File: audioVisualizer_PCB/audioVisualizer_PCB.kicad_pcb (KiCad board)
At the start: 2 copper layers, 129.1 x 32.5 mm, 40 parts, among them J1 USB_C_16P, J2 SWD_DEBUG, J3 SPI_LED_MATRIX, U1 AMS1117-3.3, U7 STM32F401CCUx, Y1 ASE-25MHz

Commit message: update
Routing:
- net +3.3V: track 322.8 -> 296.7 mm, vias 7 -> 9
- net GND: track 129.1 -> 124.5 mm, vias 22 -> 21
- net SWDIO: track 16.9 -> 15.7 mm

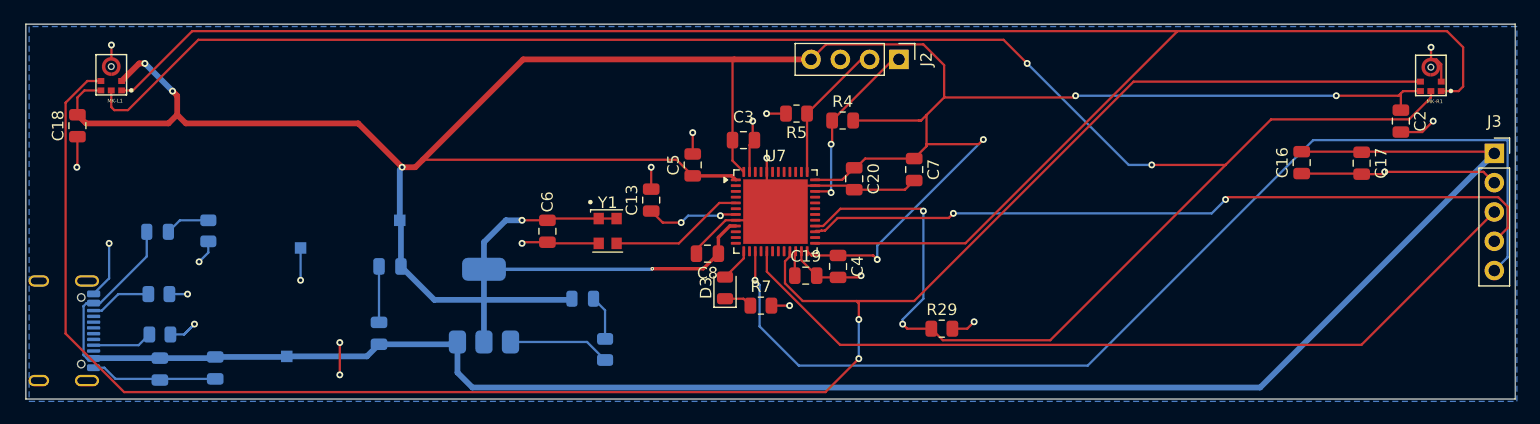
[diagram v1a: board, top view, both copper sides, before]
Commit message: update afer review; power fixed?
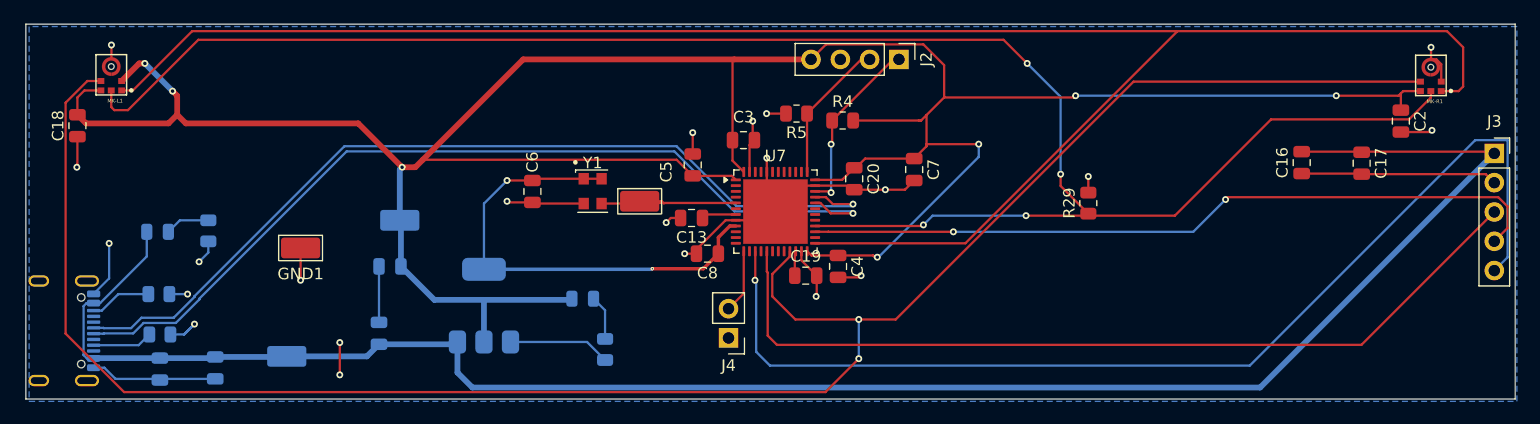
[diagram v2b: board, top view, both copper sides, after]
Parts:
- removed D3: LED, LED_SMD:LED_0805_2012Metric
- removed R7: 10Ω, Resistor_SMD:R_0805_2012Metric
- added CRYS_25: CRYS_25, TestPoint:TestPoint_Keystone_5015_Micro_Mini, F.Cu at (90.9, 65.0)
- added J4: test_con, Connector_PinHeader_2.54mm:PinHeader_1x02_P2.54mm_Vertical, F.Cu at (98.6, 76.8)
- 3V3, 5V1: footprint TestPoint:TestPoint_Pad_1.0x1.0mm -> TestPoint:TestPoint_Keystone_5015_Micro_Mini
- C13: value 100n -> 100nF
- GND1: footprint TestPoint:TestPoint_Pad_1.0x1.0mm -> TestPoint:TestPoint_Keystone_5015_Micro_Mini; moved to F.Cu
- R1, R3: value 5.1 -> 5.1k
- moved R29 16.7 mm to (129.8, 65.1), turned to 90 degrees
- moved C13 3.83 mm to (95.4, 66.4), turned to 180 degrees
- moved C6 3.69 mm to (81.6, 64.1)
- moved Y1 3.69 mm to (86.8, 64.1)
- turned GND1 to 180 degrees
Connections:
- J1 pad A6: unconnected-(J1-D+-PadA6) -> USB_D+
- J1 pad A7: unconnected-(J1-D--PadA7) -> USB_D-
- J1 pad B6: unconnected-(J1-D+-PadA6) -> USB_D+
- J1 pad B7: unconnected-(J1-D--PadA7) -> USB_D-
- U7 pad 32: unconnected-(U7-PA11-Pad32) -> USB_D+
- U7 pad 33: unconnected-(U7-PA12-Pad33) -> USB_D-
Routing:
- net USB_D+: track 0.00 -> 78.3 mm, vias 0 -> 1
- net USB_D-: track 0.00 -> 78.2 mm, vias 0 -> 1
- net MIC_SD: track 181.5 -> 158.1 mm
- net Net-(U7-NRST): track 8.04 -> 3.01 mm, vias 2 -> 0
- net SPI_DIN: track 72.2 -> 75.5 mm
- net Net-(J4-Pin_2): track 2.91 -> 5.53 mm
- net Net-(D3-K): track 2.45 -> 0.00 mm
- net GND: track 124.5 -> 122.1 mm, vias 21 -> 22
- net /CRYS_OUT: track 11.8 -> 14.0 mm
- net +3.3V: track 296.7 -> 294.6 mm
- net MIC_SCK: track 167.6 -> 169.5 mm
- net SPI_CLK: track 92.8 -> 94.3 mm

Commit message: update
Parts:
- removed J4: test_con, Connector_PinHeader_2.54mm:PinHeader_1x02_P2.54mm_Vertical
- removed U7: STM32F401CCUx, Package_DFN_QFN:QFN-48-1EP_7x7mm_P0.5mm_EP5.6x5.6mm
- added U2: STM32F401RETx, Package_QFP:LQFP-64_10x10mm_P0.5mm, F.Cu at (106.2, 67.8)
- moved C4 28.3 mm to (136.3, 72.5)
- moved C19 28.3 mm to (133.5, 73.3)
- moved R29 27.4 mm to (105.8, 51.8)
- moved J2 23.1 mm to (122.4, 73.9), turned to 180 degrees
- moved C20 17.8 mm to (126.9, 59.2)
- moved C7 17.8 mm to (132.1, 58.5)
- moved R4 17.8 mm to (125.9, 54.2)
- moved R5 17.8 mm to (121.9, 53.6)
- moved C5 16.9 mm to (103.2, 76.8), turned to 180 degrees
- moved CRYS_25 11.4 mm to (82.9, 56.9)
- moved Y1 11.4 mm to (78.8, 56.0)
- moved C6 11.4 mm to (73.6, 56.0)
- moved C8 8.06 mm to (98.4, 61.6), turned to 90 degrees
- moved C3 3.79 mm to (103.4, 58.2)
- moved R2 3.52 mm to (84.4, 78.2)
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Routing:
- net +3.3V: track 294.6 -> 0.00 mm, vias 9 -> 0
- net MIC_SCK: track 169.5 -> 0.00 mm, vias 2 -> 0
- net +5V: track 165.1 -> 0.00 mm
- net MIC_WS: track 163.5 -> 0.00 mm
- net MIC_SD: track 158.1 -> 0.00 mm, vias 4 -> 0
- net GND: track 122.1 -> 0.00 mm, vias 22 -> 0
- net SPI_CLK: track 94.3 -> 0.00 mm, vias 1 -> 0
- net USB_D+: track 78.3 -> 0.00 mm, vias 1 -> 0
- net USB_D-: track 78.2 -> 0.00 mm, vias 1 -> 0
- net SPI_DIN: track 75.5 -> 0.00 mm
- net SPI_CS: track 65.1 -> 0.00 mm, vias 2 -> 0
- net SWDIO: track 15.7 -> 0.00 mm, vias 2 -> 0
- net /CRYS_OUT: track 14.0 -> 0.00 mm
- net SWCLK: track 12.5 -> 0.00 mm
- net Net-(J4-Pin_2): track 5.53 -> 0.00 mm
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
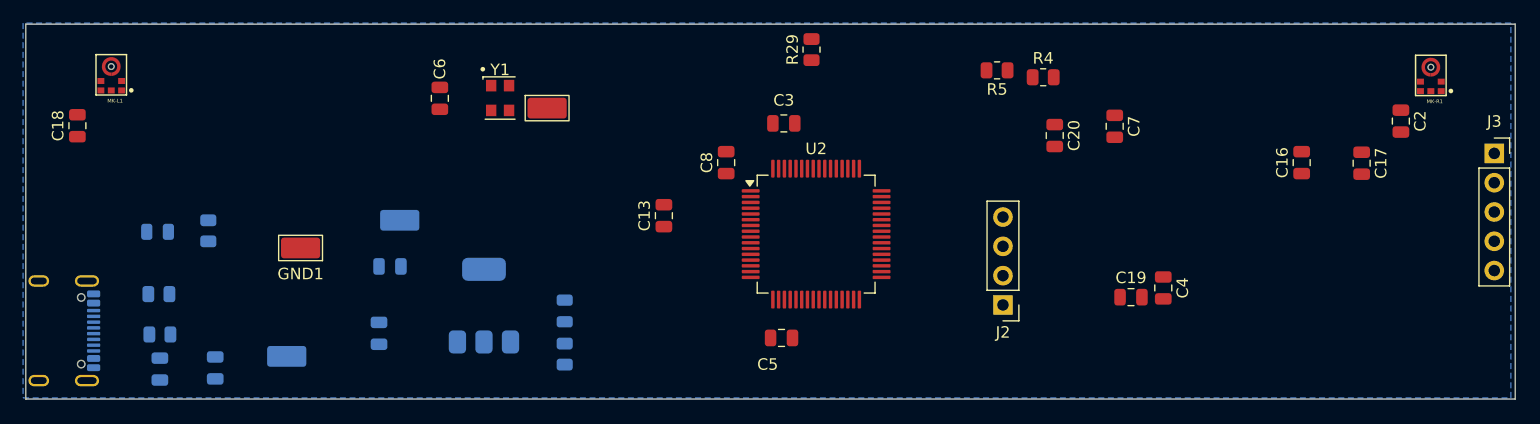
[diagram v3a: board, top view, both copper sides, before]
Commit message: new mcu
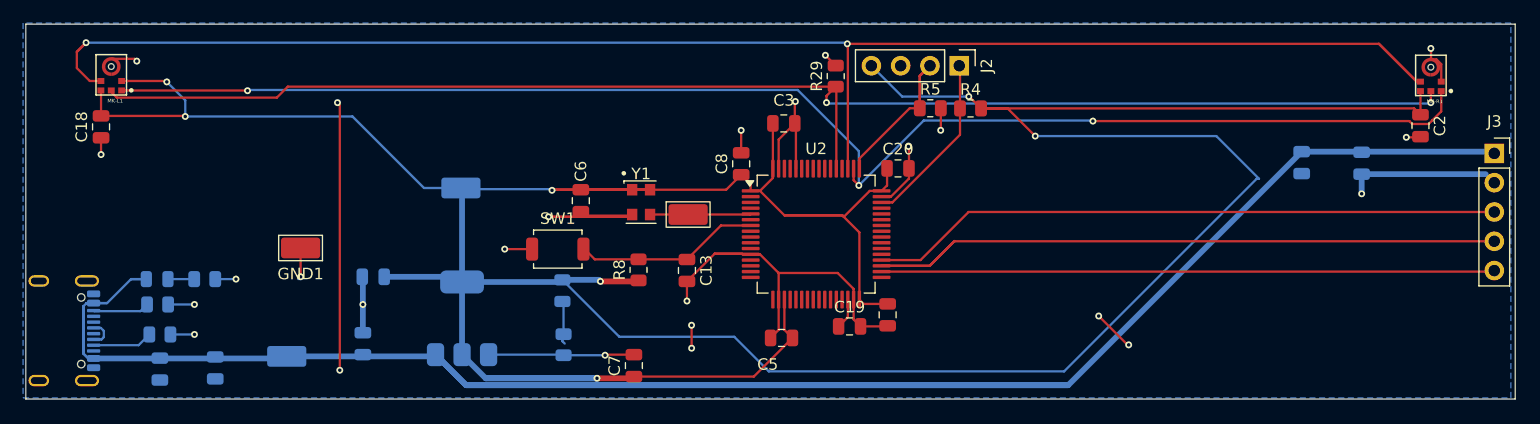
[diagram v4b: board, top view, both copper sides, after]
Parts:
- added R8: 10k, Resistor_SMD:R_0805_2012Metric, F.Cu at (90.8, 70.9)
- added SW1: SW_Push, Button_Switch_SMD:SW_SPST_TS-1088-xR020, F.Cu at (83.8, 69.1)
- C16, C17: moved to B.Cu
- moved C7 46.6 mm to (90.4, 79.2), turned to 90 degrees
- moved C19 24.5 mm to (109.1, 75.8)
- moved C4 24.0 mm to (112.4, 74.8)
- moved J2 21.1 mm to (118.6, 53.2), turned to -90 degrees
- moved CRYS_25 15.3 mm to (95.1, 66.1)
- moved Y1 15.2 mm to (91.0, 65.0)
- moved C6 15.1 mm to (85.8, 64.9)
- moved C20 13.9 mm to (113.3, 62.1), turned to 0 degrees
- moved R4 6.85 mm to (119.6, 56.9)
- moved R5 6.66 mm to (116.1, 56.9), turned to 0 degrees
- moved 3V3 5.99 mm to (75.4, 63.8)
- moved C13 5.15 mm to (95.0, 71.0), turned to -90 degrees
- moved R6 4.20 mm to (53.2, 71.7), turned to 0 degrees
- moved D2 4.10 mm to (49.1, 71.7)
- moved R29 3.11 mm to (107.9, 54.1)
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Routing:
- net +3.3V: track 0.00 -> 352.2 mm, vias 0 -> 7
- net +5V: track 0.00 -> 207.1 mm
- net GND: track 0.00 -> 152.1 mm, vias 0 -> 25
- net MIC_SCK: track 0.00 -> 139.3 mm, vias 0 -> 2
- net MIC_WS: track 0.00 -> 125.9 mm, vias 0 -> 3
- net MIC_SD: track 0.00 -> 125.9 mm, vias 0 -> 2
- net SPI_CS: track 0.00 -> 61.2 mm
- net SPI_DIN: track 0.00 -> 54.9 mm
- net SPI_CLK: track 0.00 -> 53.2 mm
- net SWCLK: track 0.00 -> 16.0 mm
- net Net-(U2-NRST): track 0.00 -> 16.0 mm
- net SWDIO: track 0.00 -> 15.2 mm
- net /CRYS_OUT: track 0.00 -> 8.75 mm
- net Net-(J1-CC1): track 0.00 -> 5.22 mm
- net Net-(J1-CC2): track 0.00 -> 4.89 mm
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
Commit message: updated actions and readme to upload pcb preview
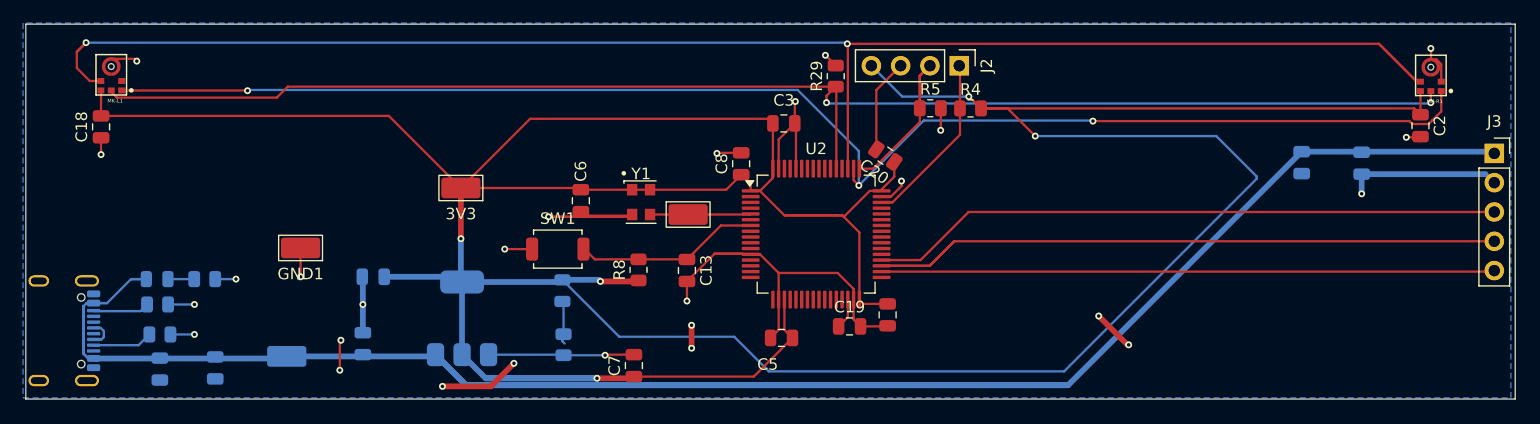
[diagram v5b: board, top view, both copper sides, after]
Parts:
- 3V3: moved to F.Cu
- moved C20 1.56 mm to (112.2, 61.0), turned to 145 degrees
- turned 3V3 to 180 degrees
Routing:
- net GND: track 152.1 -> 143.5 mm, vias 25 -> 27
- net +3.3V: track 352.2 -> 360.4 mm, vias 7 -> 5

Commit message: update
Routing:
- net +3.3V: track 360.4 -> 368.0 mm, vias 5 -> 7
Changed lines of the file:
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@@
 				(name "A")
 				(pins "7" "60" "13" "5" "6" "54" "8" "9" "10" "11" "24" "25" "37" "38"
-					"39" "40" "51" "52" "53" "2" "3" "4" "30" "1" "19" "32" "63" "31" "47"
-					"18" "48" "12" "64" "14" "15" "16" "17" "20" "21" "22" "23" "41" "42"
+					"39" "40" "51" "52" "53" "2" "3" "4" "30" "1" "19" "32" "47" "18" "63"
+					"31" "48" "12" "64" "14" "15" "16" "17" "20" "21" "22" "23" "41" "42"
 					"43" "44" "45" "46" "49" "50" "26" "27" "28" "55" "56" "57" "58" "59"
 					"61" "62" "29" "33" "34" "35" "36"
@@
 			(unit
 				(name "A")
-				(pins "SH" "B1" "B12" "A1" "A12" "A9" "B4" "B9" "A4" "A5" "B5" "A7" "B7"
+				(pins "SH" "A1" "A12" "B1" "B12" "A4" "A9" "B4" "B9" "A5" "B5" "A7" "B7"
 					"A6" "B6" "A8" "B8"
 				)
@@
 	)
 	(segment
+		(start 49.322 54.522)
+		(end 49.4 54.6)
+		(width 0.2)
+		(layer "F.Cu")
+		(net "+3.3V")
+	)
+	(segment
 		(start 69.15 57.55)
 		(end 75.4 63.8)
@@
 	)
 	(segment
+		(start 44.2 57.55)
+		(end 52.35 57.55)
+		(width 0.2)
+		(layer "F.Cu")
+		(net "+3.3V")
+	)
+	(segment
 		(start 100.525 64.05)
 		(end 101.332 64.05)
@@
 	)
 	(segment
-		(start 44.2 57.55)
+		(start 52.35 57.55)
 		(end 69.15 57.55)
 		(width 0.2)
@@
 	)
 	(segment
+		(start 45.9845 54.522)
+		(end 49.322 54.522)
+		(width 0.2)
+		(layer "F.Cu")
+		(net "+3.3V")
+	)
+	(segment
 		(start 103.45 66.1676)
 		(end 108.468 66.1676)
@@
 	)
 	(segment
+		(start 51.4 56.6)
+		(end 52.35 57.55)
+		(width 0.2)
+		(layer "F.Cu")
+		(net "+3.3V")
+	)
+	(segment
 		(start 100.525 64.05)
 		(end 100.525 63.475)
@@
 	)
 	(via
+		(at 49.4 54.6)
+		(size 0.6)
+		(drill 0.3)
+		(layers "F.Cu" "B.Cu")
+		(net "+3.3V")
+	)
+	(via
 		(at 87.5 71.9)
 		(size 0.6)
@@
 	)
 	(via
+		(at 51.4 56.6)
+		(size 0.6)
+		(drill 0.3)
+		(layers "F.Cu" "B.Cu")
+		(net "+3.3V")
+	)
+	(via
 		(at 119.4362 55.8745)
 		(size 0.6)
@@
 		(width 0.2)
 		(layer "B.Cu")
+		(net "+3.3V")
+	)
+	(segment
+		(start 49.4 54.6)
+		(end 51.4 56.6)
+		(width 0.2)
+		(layer "B.Cu")

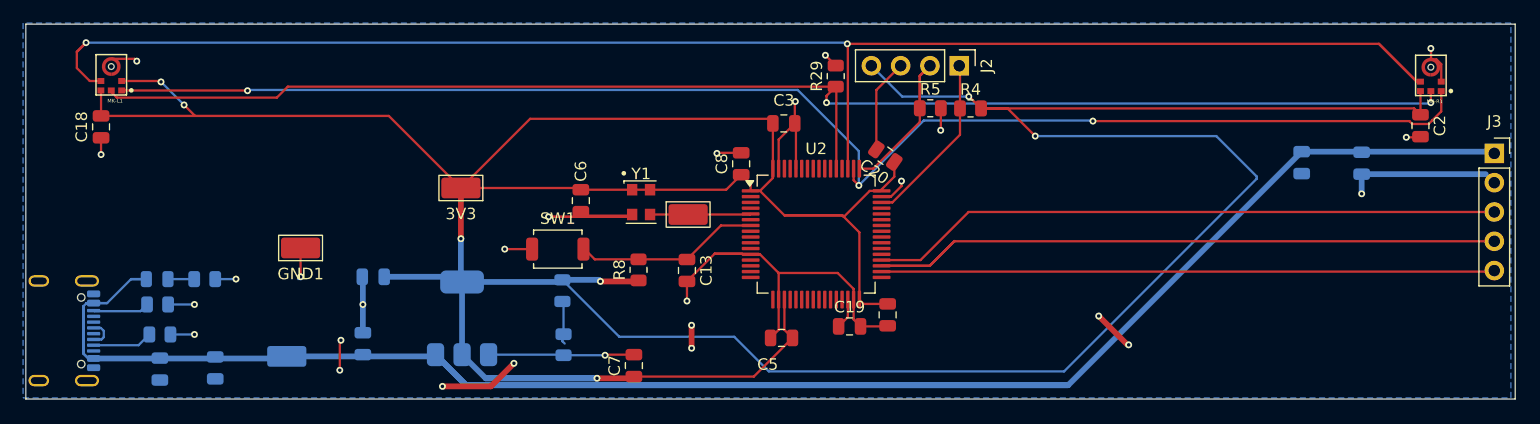
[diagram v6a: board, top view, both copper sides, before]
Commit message: updated workflow and removed production folder
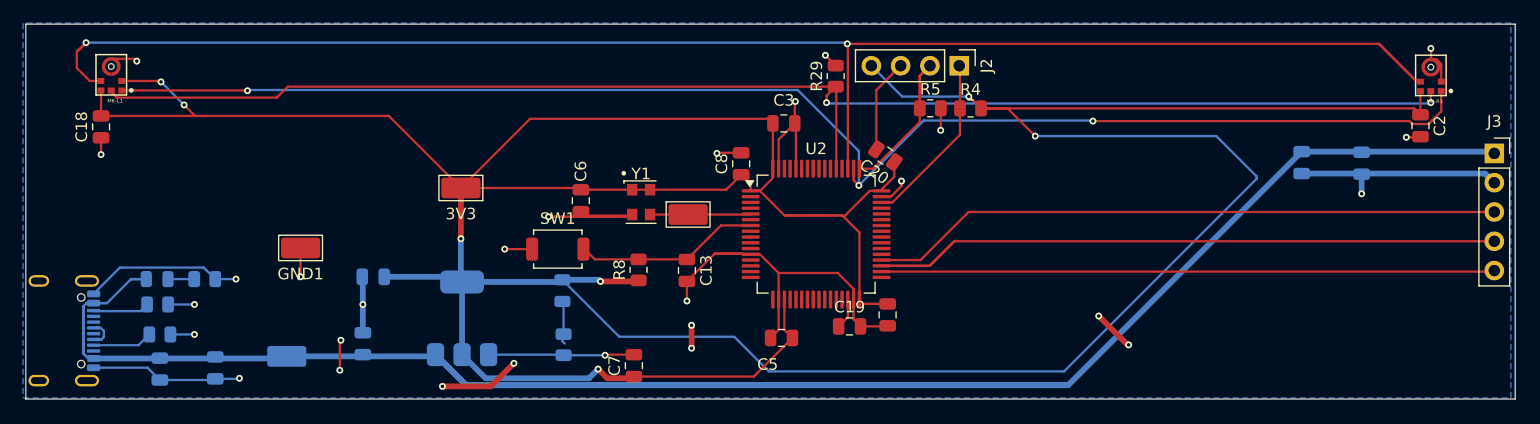
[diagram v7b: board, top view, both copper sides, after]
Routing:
- net GND: track 143.5 -> 173.7 mm, vias 27 -> 28
- net +3.3V: track 368.0 -> 359.0 mm
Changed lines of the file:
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@@
+	)
+	(segment
+		(start 87.3 79.5)
+		(end 88.1 80.3)
+		(width 0.5)
+		(layer "F.Cu")
+		(net "+3.3V")
 	)
 	(segment
@@
 	)
 	(segment
+		(start 88.1 80.3)
+		(end 90.25 80.3)
+		(width 0.5)
+		(layer "F.Cu")
+		(net "+3.3V")
+	)
+	(segment
 		(start 52.35 57.55)
 		(end 69.15 57.55)
@@
 	)
 	(segment
-		(start 87.2 80.3)
-		(end 90.25 80.3)
-		(width 0.5)
-		(layer "F.Cu")
-		(net "+3.3V")
-	)
-	(segment
 		(start 85.3 63.8)
 		(end 75.4 63.8)
@@
 	)
 	(segment
+		(start 90.25 80.3)
+		(end 90.4 80.15)
+		(width 0.5)
+		(layer "F.Cu")
+		(net "+3.3V")
+	)
+	(segment
 		(start 103.45 66.1676)
 		(end 108.468 66.1676)
@@
 	)
 	(segment
-		(start 90.25 80.3)
-		(end 90.4 80.15)
-		(width 0.5)
-		(layer "F.Cu")
-		(net "+3.3V")
-	)
-	(segment
 		(start 102.45 62.125)
 		(end 102.45 58.2)
@@
 	)
 	(via
-		(at 87.2 80.3)
+		(at 87.3 79.5)
 		(size 0.6)
 		(drill 0.3)
@@
 	)
 	(segment
+		(start 77.55 80.3)
+		(end 86.5 80.3)
+		(width 0.5)
+		(layer "B.Cu")
+		(net "+3.3V")
+	)
+	(segment
 		(start 140.9 59.3)
 		(end 144.4 62.8)
@@
 	)
 	(segment
-		(start 77.55 80.3)
-		(end 87.2 80.3)
-		(width 0.5)
-		(layer "B.Cu")
-		(net "+3.3V")
-	)
-	(segment
 		(start 127.7 79.7)
 		(end 144.4 63)
@@
 	)
 	(segment
-		(start 77.55 80.3)
-		(end 87.2 80.3)
+		(start 86.5 80.3)
+		(end 87.3 79.5)
 		(width 0.5)
 		(layer "B.Cu")
@@
 	)
 	(via
+		(at 56.2 80.3)
+		(size 0.6)
+		(drill 0.3)
+		(layers "F.Cu" "B.Cu")
+		(net "GND")
+	)
+	(via
 		(at 104.4 56.3)
 		(size 0.6)
@@
 	)
 	(segment
+		(start 43.555 72.98)
+		(end 45.835 70.7)
+		(width 0.2)
+		(layer "B.Cu")
+		(net "GND")
+	)
+	(segment
 		(start 84.3 78.3)
 		(end 87.9 78.3)
@@
 	)
 	(segment
+		(start 56.15 80.35)
+		(end 56.2 80.3)
+		(width 0.2)
+		(layer "B.Cu")
+		(net "GND")
+	)
+	(segment
+		(start 54.1 80.35)
+		(end 56.15 80.35)
+		(width 0.2)
+		(layer "B.Cu")
+		(net "GND")
+	)
+	(segment
 		(start 66.9 73.9)
 		(end 66.9 71.55)
@@
 	)
 	(segment
-		(start 164.26 62.6)
-		(end 165 63.34)
+		(start 54 80.45)
+		(end 54.1 80.35)
 		(width 0.2)
 		(layer "B.Cu")
@@
 	)
 	(segment
+		(start 43.555 79.38)
+		(end 48.23 79.38)
+		(width 0.2)
+		(layer "B.Cu")
+		(net "GND")
+	)
+	(segment
 		(start 50.0125 73.9)
 		(end 52.3 73.9)
@@
 	)
 	(segment
+		(start 48.23 79.38)
+		(end 49.3 80.45)
+		(width 0.2)
+		(layer "B.Cu")
+		(net "GND")
+	)
+	(segment
 		(start 66.9 76.35)
 		(end 66.9 73.9)
@@
 	)
 	(segment
+		(start 164.21 62.55)
+		(end 165 63.34)
+		(width 0.5)
+		(layer "B.Cu")
+		(net "GND")
+	)
+	(segment
+		(start 45.835 70.7)
+		(end 53.1 70.7)
+		(width 0.2)
+		(layer "B.Cu")
+		(net "GND")
+	)
+	(segment
+		(start 148.3 62.55)
+		(end 164.21 62.55)
+		(width 0.5)
+		(layer "B.Cu")
+		(net "GND")
+	)
+	(segment
 		(start 77.8 78.25)
 		(end 84.25 78.25)
@@
 	)
 	(segment
+		(start 49.3 80.45)
+		(end 54 80.45)
+		(width 0.2)
+		(layer "B.Cu")
+		(net "GND")
+	)
+	(segment
 		(start 153.5 62.6)
 		(end 153.5 64.3)
@@
 	)
 	(segment
+		(start 53.1 70.7)
+		(end 54.1 71.7)
+		(width 0.2)
+		(layer "B.Cu")
+		(net "GND")
+	)
+	(segment
 		(start 54.1 71.7)
 		(end 55.9 71.7)
@@
 		(layer "B.Cu")
 		(net "GND")
-	)
-	(segment
-		(start 153.5 62.6)
-		(end 164.26 62.6)
-		(width 0.5)
-		(layer "B.Cu")
-		(net "GND")

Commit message: add decoup for VREF+ pin
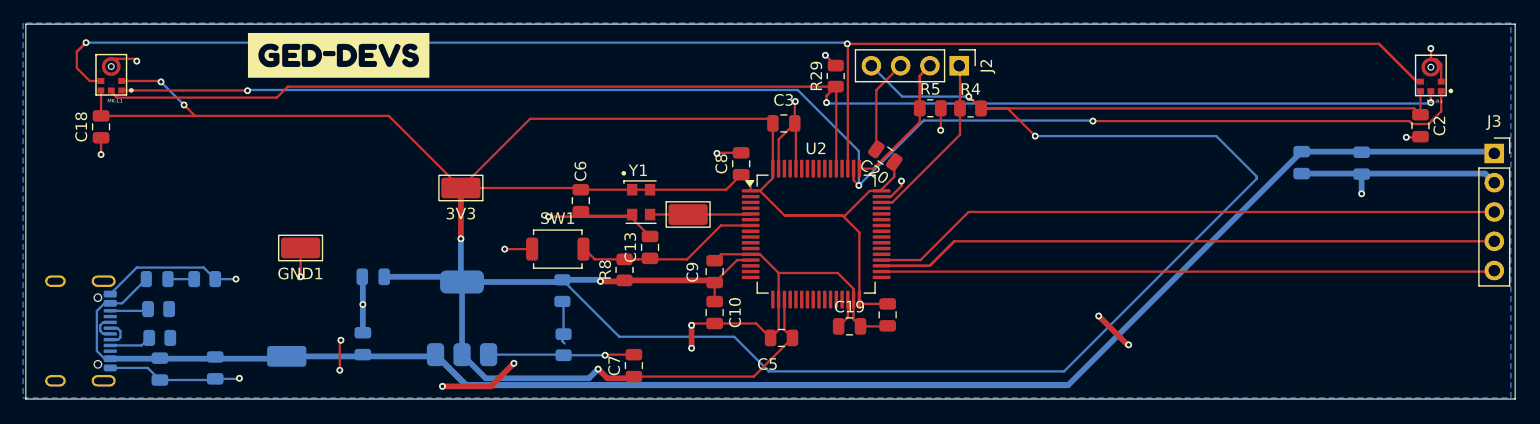
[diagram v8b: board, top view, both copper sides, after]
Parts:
- added C10: 10uF, Capacitor_SMD:C_0805_2012Metric, F.Cu at (97.4, 74.6)
- added C9: 100nF, Capacitor_SMD:C_0805_2012Metric, F.Cu at (97.4, 71.0)
- kibuzzard-69F6314F: moved to F.Cu
- moved kibuzzard-69F6314F 82.0 mm to (64.8, 52.3), turned to 0 degrees
- moved C13 3.77 mm to (91.8, 69.0), turned to 90 degrees
- moved J1 1.45 mm to (41.3, 76.2)
- moved R8 1.21 mm to (89.6, 70.9)
- moved R1 0.41 mm to (49.2, 74.3)
- moved R3 0.30 mm to (49.3, 76.8)
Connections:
- U2 pad 13: unconnected-(U2-VREF+-Pad13) -> +3.3V
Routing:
- net +3.3V: track 359.0 -> 371.2 mm
- net +5V: track 207.1 -> 197.6 mm
- net GND: track 173.7 -> 169.9 mm, vias 28 -> 25
- net USB_D+: track 0.00 -> 2.44 mm
- net Net-(J1-CC1): track 5.22 -> 3.64 mm
- net Net-(J1-CC2): track 4.89 -> 3.41 mm
